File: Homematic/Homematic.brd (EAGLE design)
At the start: 99.2 x 85 mm, 27 parts, among them IC1 3.3V, IC2 3.3V, P1 DF11-06-2DS, Q1 BS170

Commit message: Generate gerber files.
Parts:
- added F3: 3A, SparkFun-PowerIC:PTC
- D3: value SB2H100 -> MURS320; device diode:DO41-7.6 -> diode:SMC
- F1, F2: value PTCPTH -> 2A
- moved D3 4.43 mm to (4.45, 76.3), flipped to the bottom, turned to 90 degrees
- moved R2 0.70 mm to (36.9, 31.5)
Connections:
- new net N$9: D3.C, F3.P$2
- net N$7: now also F3.P$1; no longer D3.C
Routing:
- net N$9: track 0.00 -> 5.26 mm
- net +24V: track 11.0 -> 7.07 mm
- net N$7: track 31.2 -> 34.3 mm
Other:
- board text removed: "+24V"

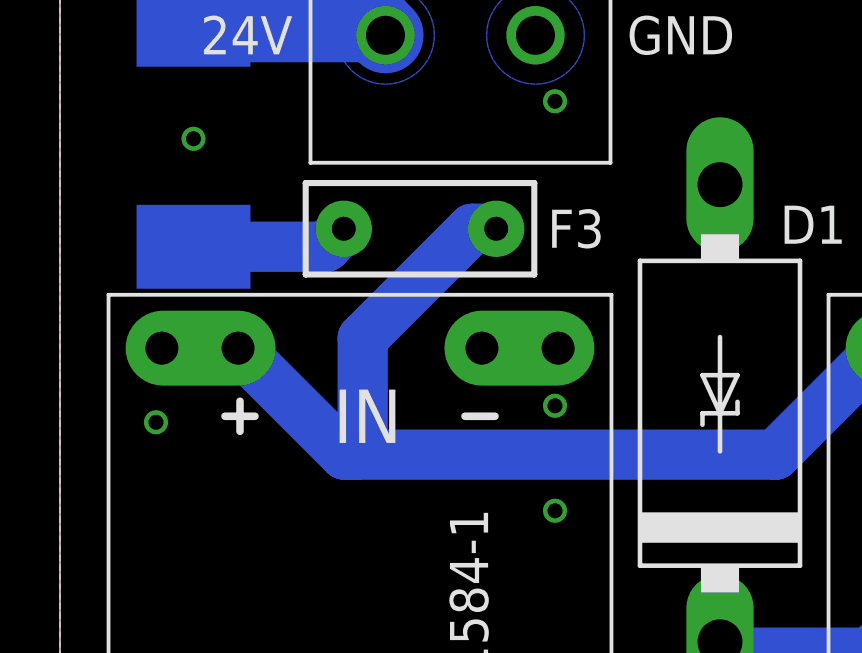
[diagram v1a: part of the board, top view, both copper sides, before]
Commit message: Fix PTC size.
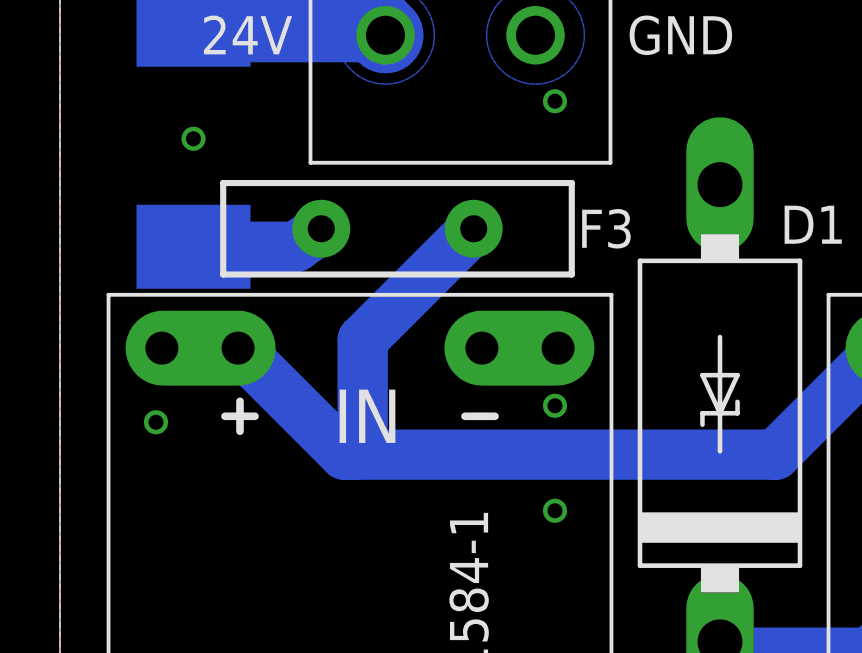
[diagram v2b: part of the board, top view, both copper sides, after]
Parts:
- F1, F2: device SparkFun-PowerIC:PTC -> SparkFun-Fuses:PTH
- F3: device SparkFun-PowerIC:PTC -> SparkFun-Fuses:PTH_11MM
- moved F3 0.75 mm to (11.2, 73.2)
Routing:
- net N$9: track 5.26 -> 4.45 mm
- net N$7: track 34.3 -> 33.6 mm
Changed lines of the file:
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@@
 <rectangle x1="22" y1="18" x2="24.7" y2="22" layer="42"/>
 <rectangle x1="26.5" y1="29.45" x2="28" y2="31" layer="42"/>
-<wire x1="14.6" y1="74.065" x2="9.4" y2="74.065" width="0.254" layer="42"/>
+<wire x1="13.85" y1="74.095" x2="8.65" y2="74.095" width="0.254" layer="42"/>
+<wire x1="9.03" y1="73.925" x2="3.83" y2="73.925" width="0.254" layer="42"/>
+<wire x1="2.68" y1="73.285" x2="2.68" y2="70.235" width="0.254" layer="42"/>
 </plain>
 <attributes>
@@
 <attribute name="VALUE" x="1.529" y="74.318" size="1.27" layer="28" ratio="10" rot="MR90"/>
 </element>
-<element name="F1" library="SparkFun-PowerIC" package="PTC" value="2A" x="22" y="52.3" smashed="yes" rot="R270">
+<element name="F1" library="SparkFun-Fuses" package="PTH" value="2A" x="22" y="52.3" smashed="yes" rot="R270">
 <attribute name="NAME" x="23.705" y="56.11" size="1.27" layer="25" font="vector" ratio="10" rot="R270"/>
-<attribute name="VALUE" x="19.86" y="56.11" size="0.4318" layer="27" rot="R270"/>
-</element>
-<element name="F2" library="SparkFun-PowerIC" package="PTC" value="2A" x="6" y="44.3" smashed="yes" rot="R270">
+<attribute name="VALUE" value="2A" x="19.86" y="56.11" size="0.4318" layer="27" rot="R270"/>
+</element>
+<element name="F2" library="SparkFun-Fuses" package="PTH" value="2A" x="6" y="44.3" smashed="yes" rot="R270">
 <attribute name="NAME" x="7.705" y="48.11" size="1.27" layer="25" font="vector" ratio="10" rot="R270"/>
-<attribute name="VALUE" x="3.86" y="48.11" size="0.4318" layer="27" rot="R270"/>
+<attribute name="VALUE" value="2A" x="3.86" y="48.11" size="0.4318" layer="27" rot="R270"/>
 </element>
 <element name="IC1" library="adafruit" package="TO92" value="3.3V" x="34.37" y="41.93" smashed="yes">
@@
 <attribute name="VALUE" x="19.952" y="37.601" size="1.27" layer="27" ratio="10" rot="R270"/>
 </element>
-<element name="F3" library="SparkFun-PowerIC" package="PTC" value="3A" x="12" y="73.25" smashed="yes" rot="R180">
-<attribute name="NAME" x="16.25" y="73.25" size="1.27" layer="25" font="vector" ratio="10" rot="R180" align="center-right"/>
-<attribute name="VALUE" x="15.81" y="75.39" size="0.4318" layer="27" rot="R180"/>
+<element name="F3" library="SparkFun-Fuses" package="PTH_11MM" value="3A" x="11.25" y="73.25" smashed="yes" rot="R180">
+<attribute name="NAME" x="17.25" y="73.25" size="1.27" layer="25" font="vector" ratio="10" rot="R180" align="center-right"/>
+<attribute name="VALUE" x="15.06" y="75.39" size="0.4318" layer="27" rot="R180"/>
 </element>
 </elements>
@@
 <wire x1="23.845" y1="65.72" x2="27.396" y2="69.271" width="1.6764" layer="16"/>
 <contactref element="F3" pad="P$1"/>
-<wire x1="14.54" y1="73.25" x2="13.74" y2="73.25" width="1.6764" layer="16"/>
-<wire x1="13.74" y1="73.25" x2="10.09" y2="69.6" width="1.6764" layer="16"/>
-<wire x1="10.09" y1="69.6" x2="10.09" y2="65.96" width="1.6764" layer="16"/>
 <wire x1="10.09" y1="65.96" x2="9.85" y2="65.72" width="1.6764" layer="16"/>
+<wire x1="10.09" y1="65.96" x2="10.09" y2="69.55" width="1.6764" layer="16"/>
+<wire x1="10.09" y1="69.55" x2="13.79" y2="73.25" width="1.6764" layer="16"/>
 </signal>
 <signal name="N$9">
 <contactref element="D3" pad="C"/>
 <contactref element="F3" pad="P$2"/>
-<wire x1="4.45" y1="72.65" x2="8.86" y2="72.65" width="1.6764" layer="16"/>
-<wire x1="8.86" y1="72.65" x2="9.46" y2="73.25" width="1.6764" layer="16"/>
+<wire x1="4.45" y1="72.65" x2="7.86" y2="72.65" width="1.6764" layer="16"/>
+<wire x1="7.86" y1="72.65" x2="8.71" y2="73.25" width="1.6764" layer="16"/>
 </signal>
 </signals>

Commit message: Place CC1101 on bottom.
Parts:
- moved IC2 23.8 mm to (28.0, 36.5), turned to 270 degrees
- moved C4 18.1 mm to (21.7, 38.9), turned to 180 degrees
- moved C5 14.0 mm to (32.0, 31.9), turned to 0 degrees
- moved C7 4.40 mm to (20.2, 32.5), turned to 0 degrees
- moved R2 3.65 mm to (36.9, 35.1)
- moved Q1 3.07 mm to (20.5, 28.2)
- moved R1 3.03 mm to (21.8, 24.8)
- moved C2 1.15 mm to (29.8, 43.1)
- moved R3 0.78 mm to (20.2, 35.2), turned to 0 degrees
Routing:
- net N$10: track 54.0 -> 28.9 mm
- net +3V3: track 44.4 -> 25.9 mm
- net +5V: track 103.3 -> 87.9 mm
- net N$15: track 22.2 -> 23.4 mm
- net N$11: track 5.31 -> 6.13 mm
- net N$3: track 8.07 -> 7.35 mm

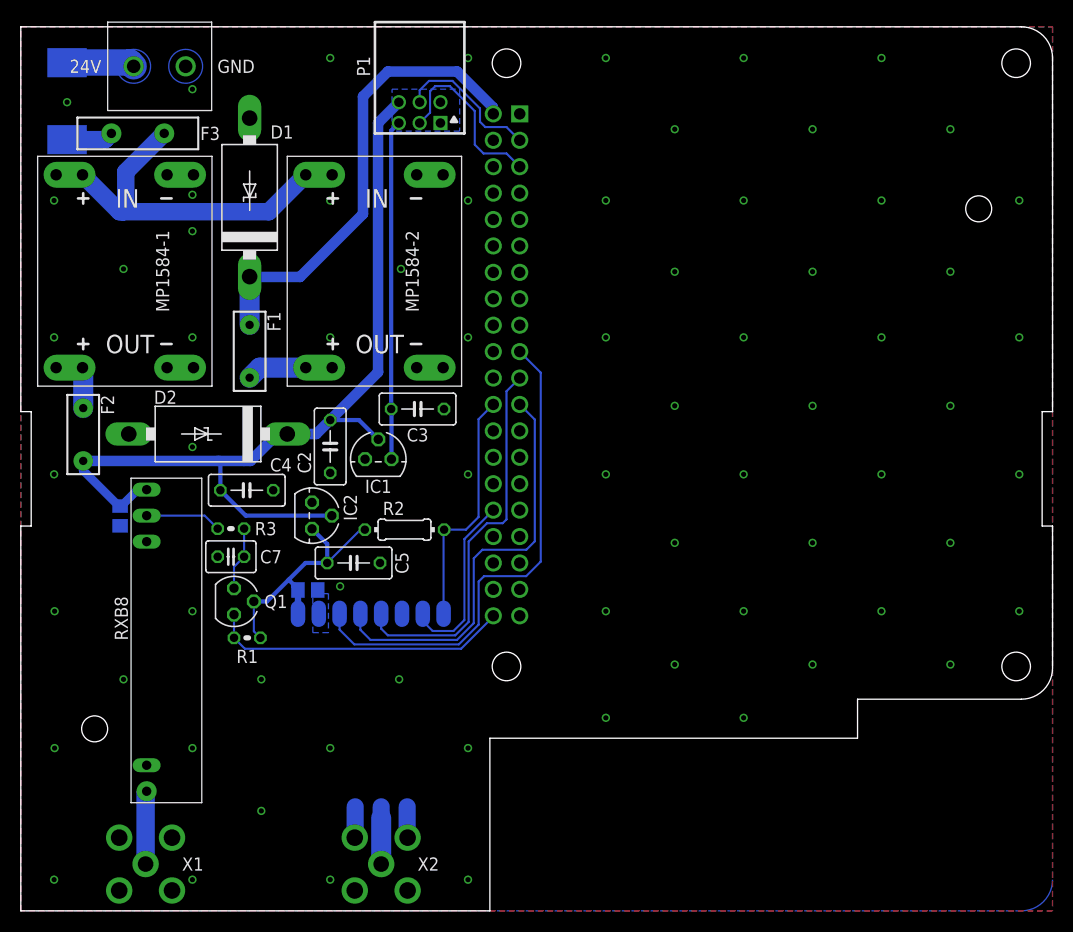
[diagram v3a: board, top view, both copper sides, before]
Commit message: Replace RXB8 with CC1101 receiver.
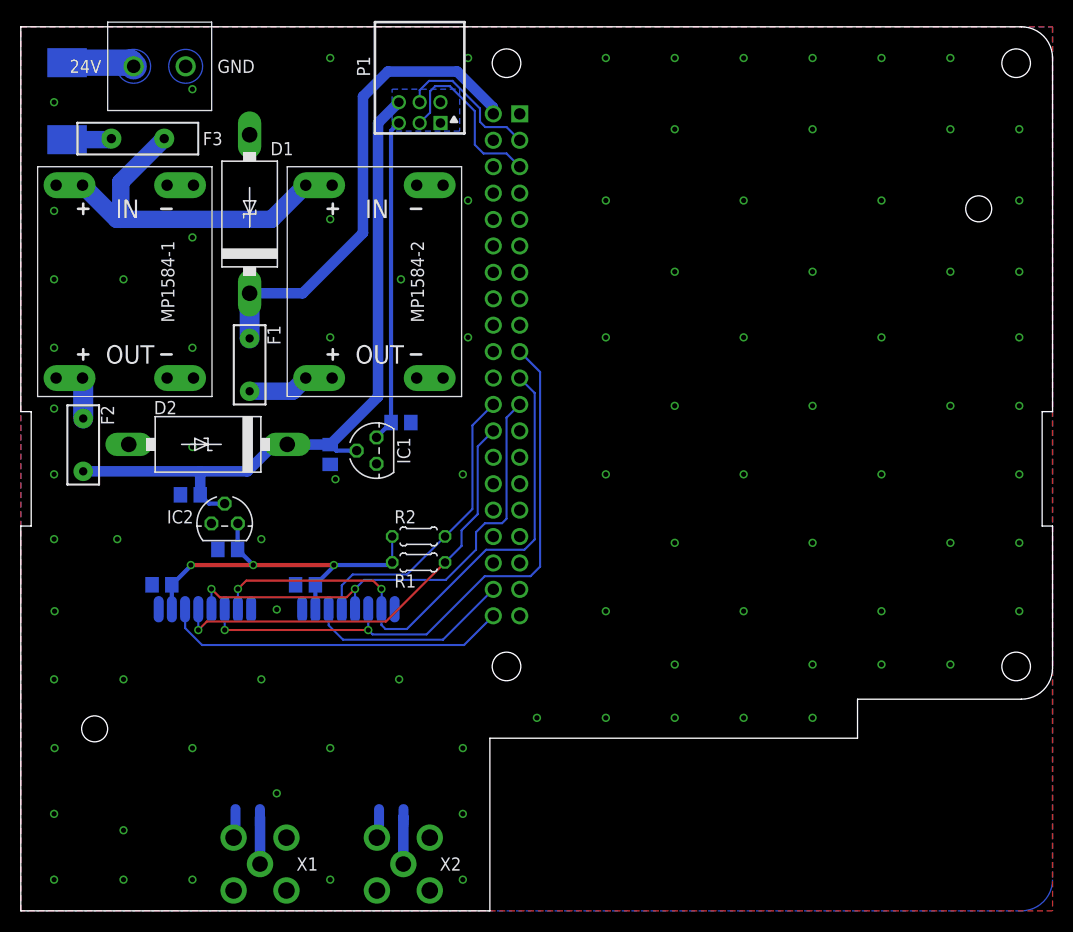
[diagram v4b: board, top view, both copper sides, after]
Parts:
- removed C7: 100nF, capacitor-wima:C2.5-3
- removed CC1101: CC1101SMD, modules:CC1101-SMD
- removed Q1: BS170, transistor-small-signal:SOT54E
- removed R3: 100R, rcl:0204V
- removed RXB8: WIRELESS-RXB8-5V, modules:WIRELESS-RXB8-5V
- added 433MHZ, 868MHZ: CC1101E07-SMD, modules:E07-M1101S-SMD
- C2, C3, C4, C5: device capacitor-wima:C5B3 -> rcl:C0805
- R1: device rcl:0204V -> rcl:0204/5
- R2: device rcl:0204/7 -> rcl:0204/5
- moved R1 18.0 mm to (38.2, 32.0)
- moved C5 12.2 mm to (19.9, 33.2), flipped to the bottom
- moved X1 11.0 mm to (23.0, 3.00)
- moved IC2 8.43 mm to (19.6, 35.8), turned to 0 degrees
- moved C1 7.74 mm to (13.6, 29.9), turned to 0 degrees
- moved C4 5.45 mm to (16.3, 38.5), flipped to the bottom
- moved X2 2.13 mm to (36.8, 3.00)
- moved C3 2.06 mm to (36.5, 45.5), flipped to the bottom, turned to 180 degrees
- moved D1 1.60 mm to (22.0, 65.5)
- moved R2 1.51 mm to (38.2, 34.5)
- moved F1 1.30 mm to (22.0, 51.0)
- moved D2 1.00 mm to (18.0, 43.4)
- moved F2 1.00 mm to (6.00, 43.3)
- moved MP1584-1 1.00 mm to (10.0, 59.0)
- moved MP1584-2 1.00 mm to (34.0, 59.0)
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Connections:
- removed net N$11: C7.2, Q1.D, R3.2
- net +3V3: now also 433MHZ.VCC, 868MHZ.VCC, C1.1, R1.1; no longer CC1101.VCC, Q1.G, R1.2
- net +5V: no longer C1.1, RXB8.VDD@1
- net GND: now also 433MHZ.GND0, 433MHZ.GND1, 868MHZ.GND0, 868MHZ.GND1; no longer C7.1, CC1101.GND0, CC1101.GND1, CC1101.GND2, RXB8.GND@1, RXB8.GND@2
- net N$10: now also 433MHZ.GDO0; no longer Q1.S, R1.1
- net N$15: now also 868MHZ.CSN; no longer CC1101.CSN
- net N$16: now also 433MHZ.SCLK, 868MHZ.SCLK; no longer CC1101.SCLK
- net N$17: now also 433MHZ.SO, 868MHZ.SO; no longer CC1101.SO
- net N$18: now also 433MHZ.SI, 868MHZ.SI; no longer CC1101.SI
- net N$19: now also 868MHZ.GDO0, RPI.38; no longer CC1101.GDO0, RPI.32
- net N$20: now also 868MHZ.ANT; no longer CC1101.ANT
- net N$3: now also 433MHZ.CSN, R1.2, RPI.26; no longer R3.1, RXB8.DATA
- net N$8: now also 433MHZ.ANT; no longer RXB8.ANT
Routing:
- net N$3: track 7.35 -> 42.9 mm, vias 0 -> 1
- net +5V: track 87.9 -> 68.2 mm
- net N$17: track 37.0 -> 54.5 mm, vias 0 -> 2
- net +3V3: track 25.9 -> 36.8 mm, vias 0 -> 3
- net N$18: track 48.2 -> 58.7 mm, vias 0 -> 2
- net N$16: track 40.9 -> 48.3 mm, vias 0 -> 2
- net N$11: track 6.13 -> 0.00 mm
- net N$15: track 23.4 -> 28.8 mm
- net N$10: track 28.9 -> 33.3 mm
- net N$19: track 17.3 -> 20.0 mm
- net N$8: track 7.04 -> 4.50 mm
- net N$2: track 32.6 -> 31.1 mm
- net N$5: track 44.9 -> 46.3 mm
- net +24V: track 7.07 -> 6.54 mm

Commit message: Fix export. Remove switch. Prepare board for production.
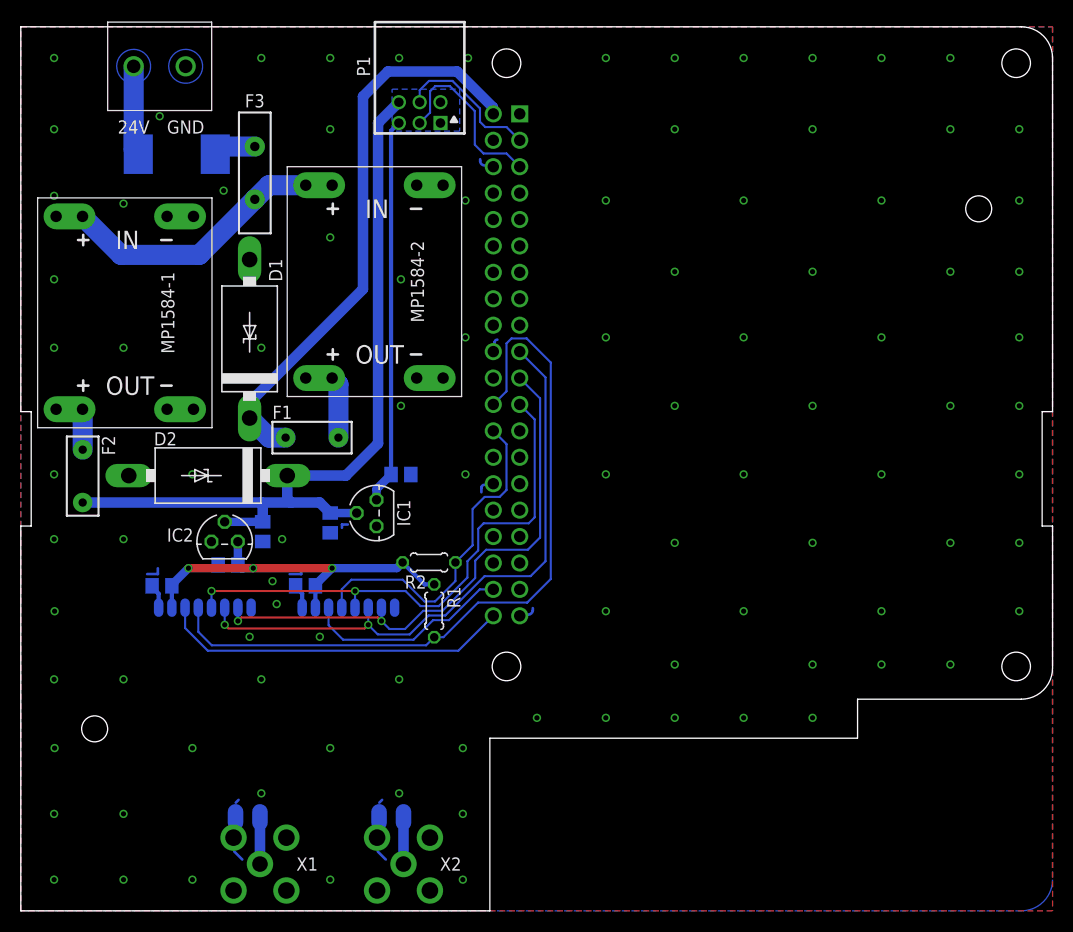
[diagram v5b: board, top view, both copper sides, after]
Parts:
- moved D1 12.0 mm to (22.0, 53.5)
- moved F3 11.7 mm to (22.5, 69.5), turned to 90 degrees
- moved D3 11.7 mm to (15.0, 71.2), turned to 0 degrees
- moved F1 9.22 mm to (28.0, 44.0), turned to 0 degrees
- moved C4 7.81 mm to (23.3, 35.0), turned to 90 degrees
- moved C2 6.58 mm to (29.8, 35.8)
- moved IC1 6.00 mm to (34.2, 36.8)
- moved C3 5.00 mm to (36.5, 40.5)
- moved R1 4.89 mm to (39.8, 27.4), turned to 270 degrees
- moved F2 3.00 mm to (5.95, 40.3)
- moved D2 3.00 mm to (18.0, 40.4)
- moved MP1584-1 3.00 mm to (10.0, 56.0)
- moved R2 2.69 mm to (39.2, 32.0)
- moved IC2 1.75 mm to (19.6, 34.0)
- moved C5 1.50 mm to (19.9, 31.8)
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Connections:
- net N$15: now also RPI.26; no longer RPI.24
- net N$3: now also RPI.24; no longer RPI.26
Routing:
- net N$3: track 42.9 -> 72.0 mm, vias 1 -> 0
- net GND: track 0.00 -> 14.1 mm, vias 89 -> 96
- net +5V: track 68.2 -> 78.7 mm
- net N$5: track 46.3 -> 55.2 mm
- net N$7: track 33.7 -> 25.8 mm
- net N$2: track 31.1 -> 37.1 mm
- net N$15: track 28.8 -> 32.6 mm
- net N$16: track 48.3 -> 52.0 mm
- net +24V: track 6.54 -> 8.64 mm
- net N$17: track 54.5 -> 53.2 mm
- net +3V3: track 36.8 -> 37.5 mm
- net N$10: track 33.3 -> 33.9 mm
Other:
- board text added: "Automation board. Version 1.2"
- board text removed: "Homematic"
